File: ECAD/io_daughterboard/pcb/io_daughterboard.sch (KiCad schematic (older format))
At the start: 80 parts, among them P1 CONN_02X32, P2 CONN_02X32

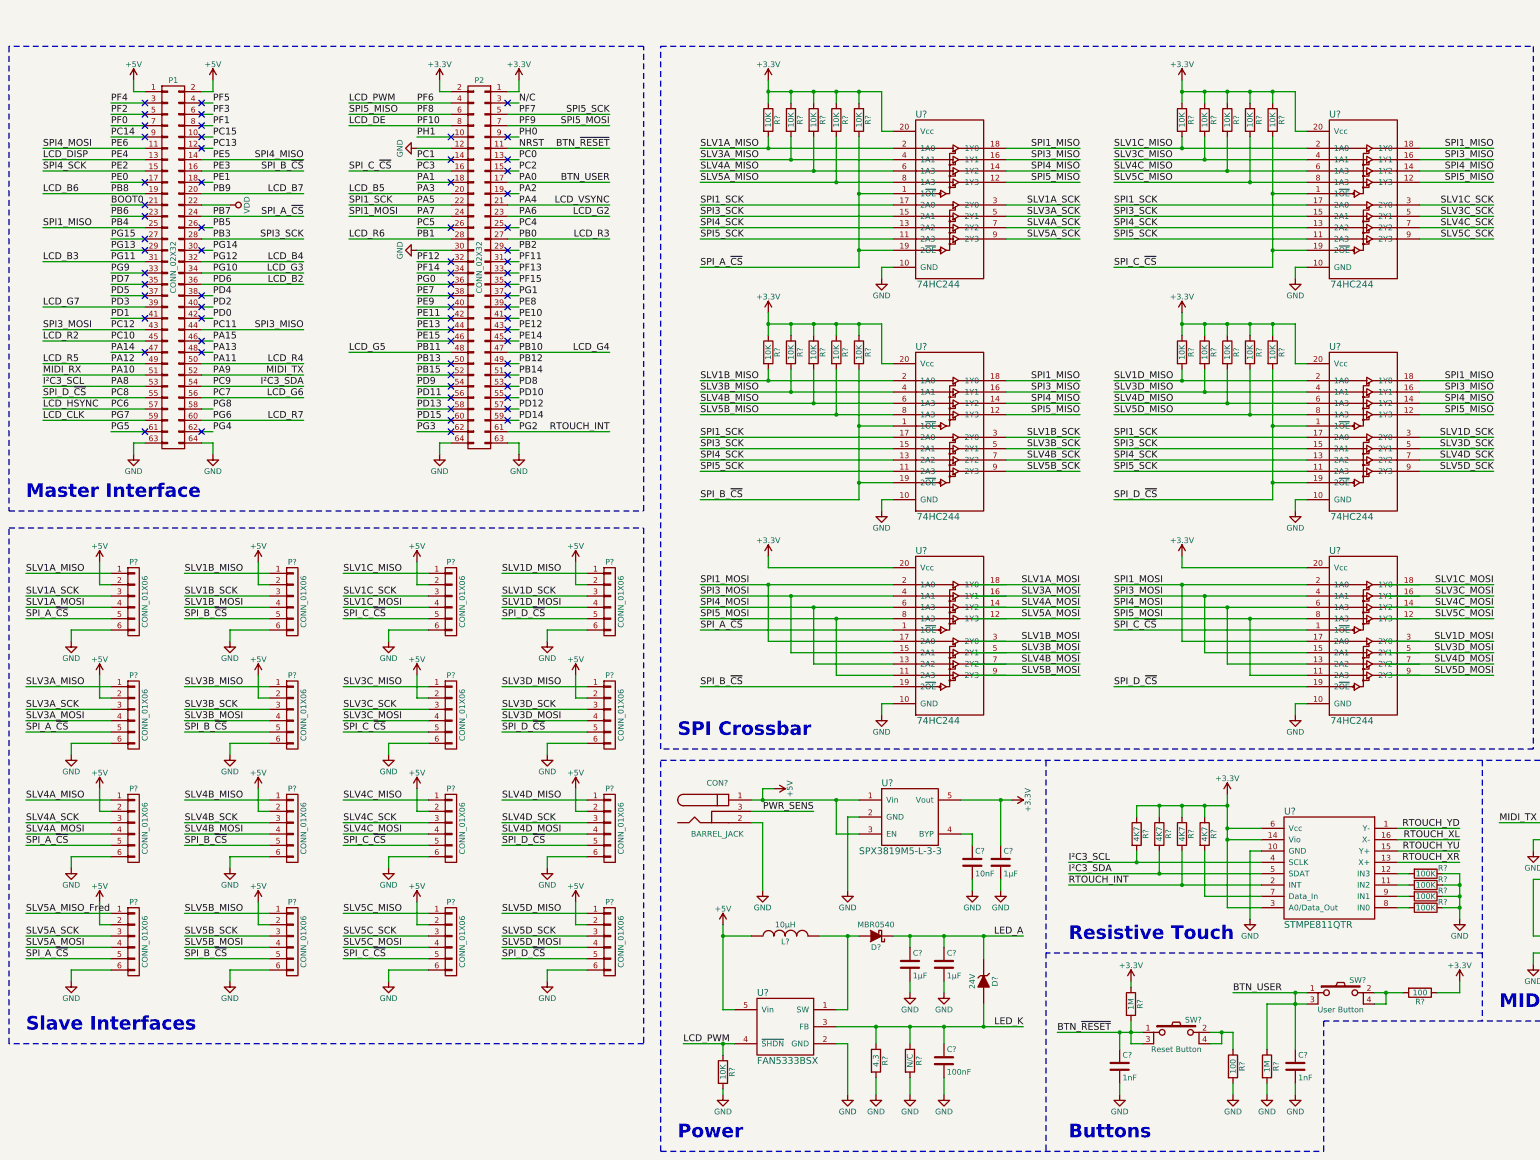
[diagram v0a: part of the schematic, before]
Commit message: Fixed 10 errors on schematic.  Still no power flags.
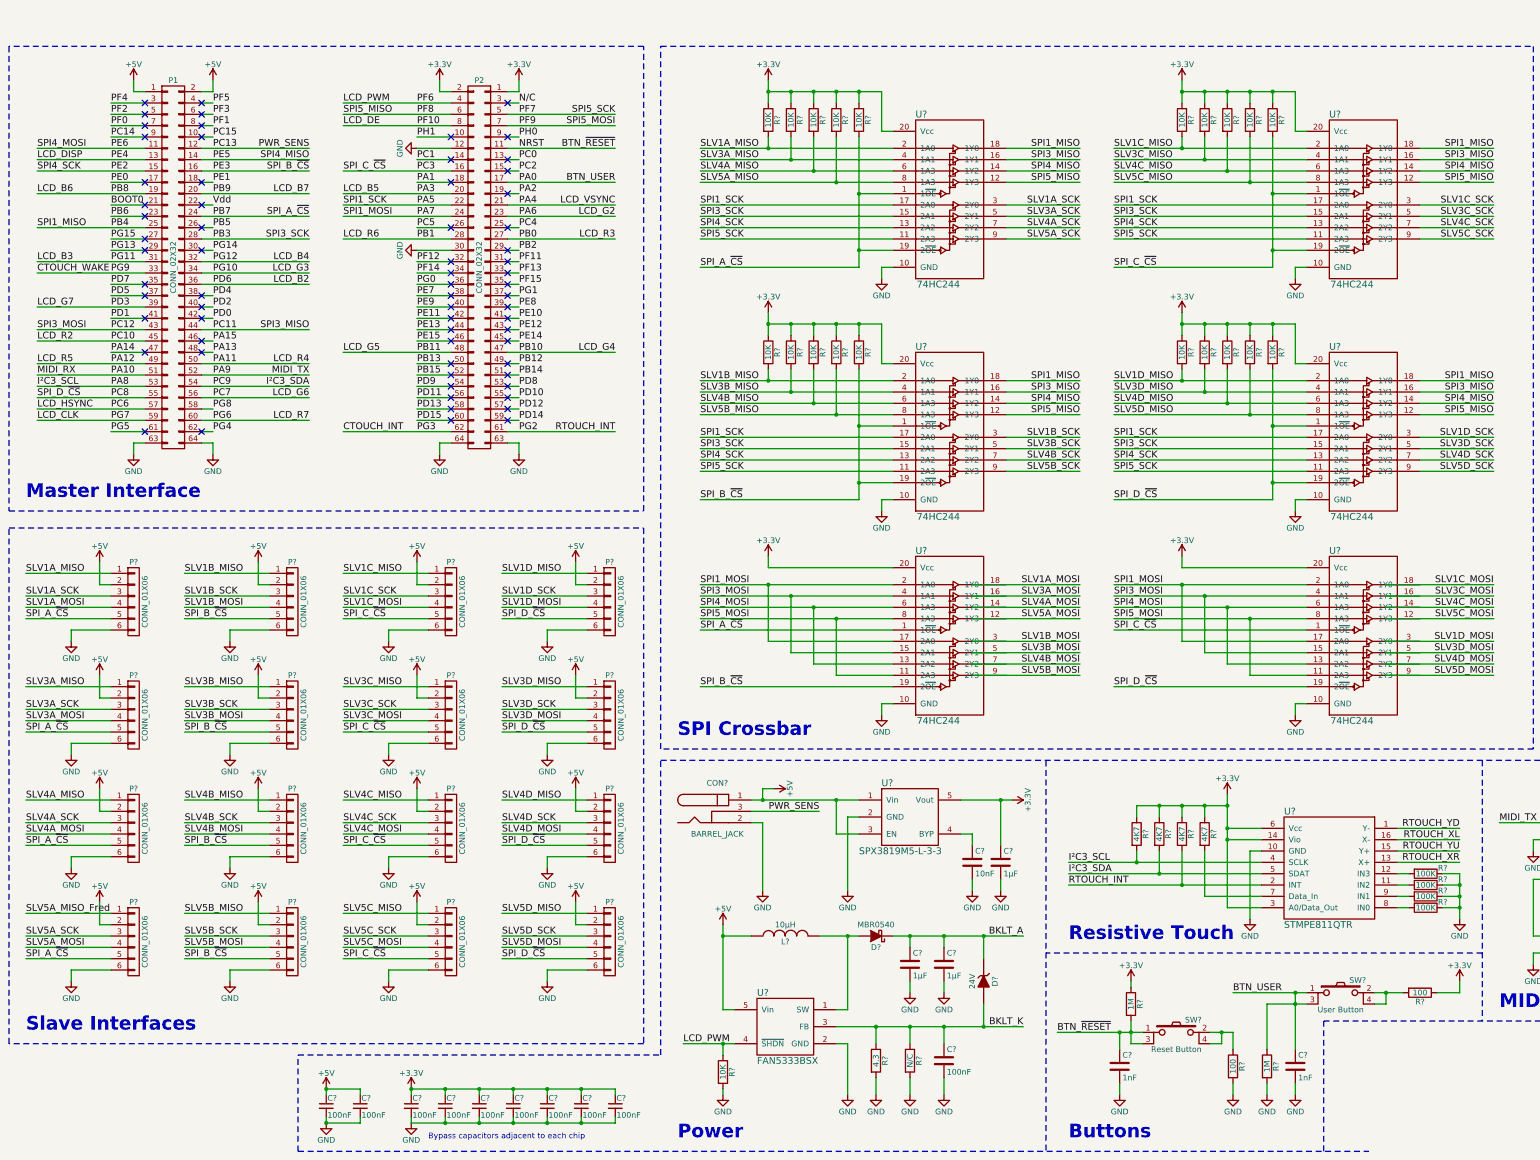
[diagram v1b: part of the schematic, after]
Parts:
- added C? (x9): 100nF, symbol C_Small
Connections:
- net LED_A is gone; now on net BKLT_A: C?.1, C?.1, D?.1 (K), D?.1 (K)
- net LED_K is gone; now on net BKLT_K: C?.1, D?.2 (A), R?.1, R?.1, U?.3 (FB)
- net PG3 is gone; now on net CTOUCH_INT: P2.62 (P62)
- net PG9 is gone; now on net CTOUCH_WAKE: P1.33 (P33)
- net PWR_SENS is gone; now on net PC13: CON?.3
- net +3V3: now also C?.1, C?.1, C?.1, C?.1, C?.1, C?.1, C?.1
- net +5V: now also C?.1, C?.1
- net GND: now also C?.2, C?.2, C?.2, C?.2, C?.2, C?.2, C?.2, C?.2, C?.2
- net VDD renamed Vdd
- no-connect marks 70 -> 68
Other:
- note added: "Bypass capacitors adjacent to each chip"

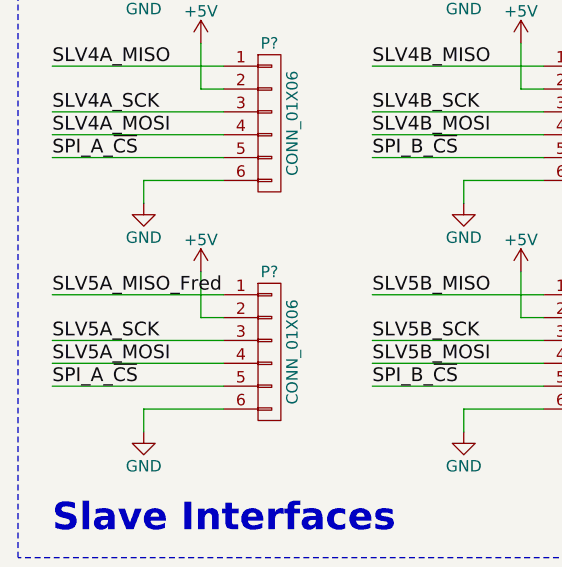
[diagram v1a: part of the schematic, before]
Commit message: Changed `SL5A_MISO_Fred` to `SL5A_MISO`.
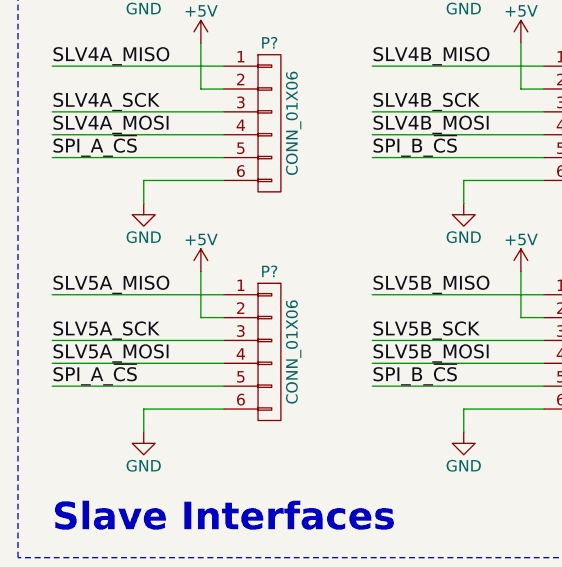
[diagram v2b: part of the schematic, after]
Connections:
- net SLV5A_MISO_Fred is gone; now on net SLV5A_MISO: P?.1 (P1)
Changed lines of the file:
@@
 $EndComp
 Text Label 800  8250 0    60   ~ 0
-SLV5A_MISO_Fred
+SLV5A_MISO
 Text Label 800  8450 0    60   ~ 0
 SLV5A_SCK

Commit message: Schematic annotated and electrical rules checked.
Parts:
- gave numbers to parts that had none: 87
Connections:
- net LCD_B6 is gone; now on net LCD_B0: J2.27 (B6), P1.19 (P19)
- net LCD_B7 is gone; now on net LCD_B1: J2.28 (B7), P1.20 (P20)
- net LCD_G6 is gone; now on net LCD_G0: J2.19 (G6), P1.56 (P56)
- net LCD_G7 is gone; now on net LCD_G1: J2.20 (G7), P1.39 (P39)
- net LCD_R6 is gone; now on net LCD_R0: J2.11 (R6), P2.28 (P28)
- net LCD_R7 is gone; now on net LCD_R1: J2.12 (R7), P1.60 (P60)
- net SLV1A_MOSI: now also U5.18 (1Y0)
- net SLV1B_MOSI: now also U5.3 (2Y0)
- net SLV1C_MOSI: now also U9.18 (1Y0)
- net SLV1D_MOSI: now also U9.3 (2Y0)
- net SLV3A_MOSI: now also U5.16 (1Y1)
- net SLV3B_MOSI: now also U5.5 (2Y1)
- net SLV3C_MOSI: now also U9.16 (1Y1)
- net SLV3D_MOSI: now also U9.5 (2Y1)
- net SLV4A_MOSI: now also U5.14 (1Y2)
- net SLV4B_MOSI: now also U5.7 (2Y2)
- net SLV4C_MOSI: now also U9.14 (1Y2)
- net SLV4D_MOSI: now also U9.7 (2Y2)
- net SLV5A_MOSI: now also U5.12 (1Y3)
- net SLV5B_MOSI: now also U5.9 (2Y3)
- net SLV5C_MOSI: now also U9.12 (1Y3)
- net SLV5D_MOSI: now also U9.9 (2Y3)
- no-connect marks 68 -> 69

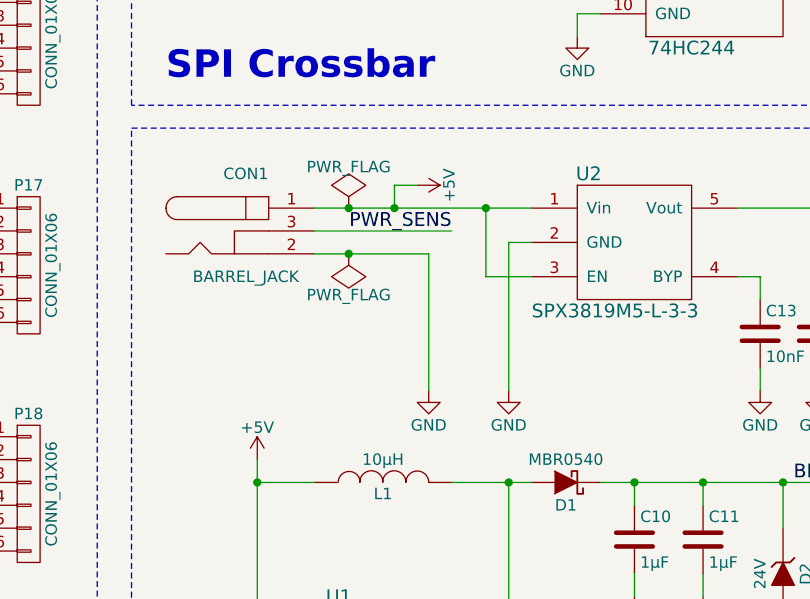
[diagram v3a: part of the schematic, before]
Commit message: Added footprints for the easy components.
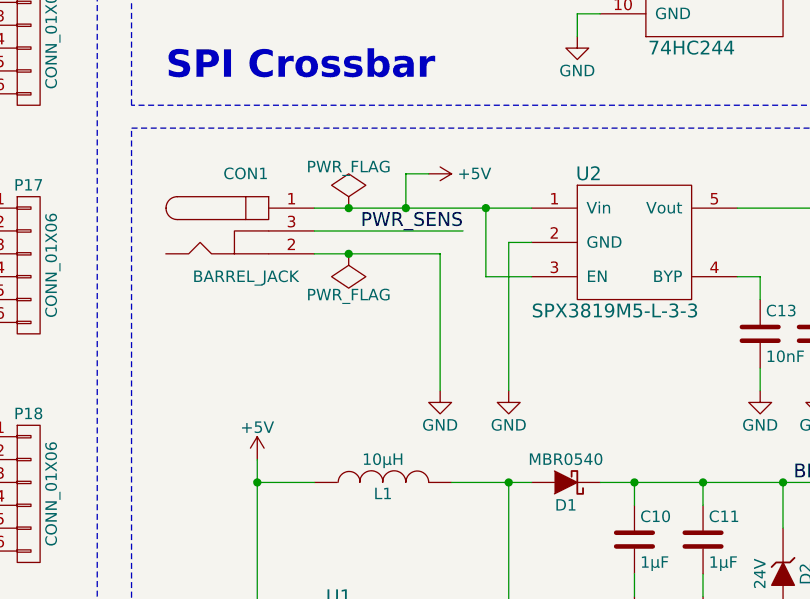
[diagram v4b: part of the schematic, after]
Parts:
- C1, C12, C13, C14, C15, C16, C2, C3, C4, C5, C6, C7, C8, C9: footprint (none) -> Capacitors_SMD:C_0603
- C10, C11: footprint (none) -> Capacitors_SMD:C_0805
- CON1: footprint (none) -> Connect:BARREL_JACK
- D1: footprint (none) -> Diodes_SMD:SOD-123
- D2: footprint (none) -> Diodes_SMD:SOD-323
- P1, P2: footprint (none) -> Socket_Strips:Socket_Strip_Straight_2x32
- R1, R10, R11, R14, R15, R16, R17, R18, R19, R2, R20, R21, R22, R23, R24, R25, R26, R27, R28, R29, R3, R30, R31, R32, R33, R34, R35, R4, R5, R6, R7, R8, R9: footprint (none) -> Resistors_SMD:R_0603
- R12, R13: footprint (none) -> Resistors_SMD:R_0603_HandSoldering
- U1, U10, U11, U2: footprint (none) -> TO_SOT_Packages_SMD:SOT-23-5
- U3, U4, U5, U7, U8, U9: footprint (none) -> Housings_SSOP:TSSOP-20_4.4x6.5mm_Pitch0.65mm
- U6: footprint (none) -> Housings_DFN_QFN:QFN-16-1EP_3x3mm_Pitch0.5mm

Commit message: Added I/O Daughter Board footprints.
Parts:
- J1: footprint (none) -> daughterfeet:XF2L-0625
- J2: footprint (none) -> daughterfeet:FPC_40
- L1: footprint (none) -> Inductors:Inductor_Taiyo-Yuden_NR-60xx
- P10, P11, P12, P13, P14, P15, P16, P17, P18, P3, P4, P5, P6, P7, P8, P9: footprint (none) -> daughterfeet:B6B-PH-SM4-TB
- P19: footprint (none) -> daughterfeet:B4B-PH-SM4-TB
- SW1, SW2: footprint (none) -> daughterfeet:WS-TASV
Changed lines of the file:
@@
 F 0 "P3" H 1750 5850 50  0000 C CNN
 F 1 "CONN_01X06" V 1850 5500 50  0000 C CNN
-F 2 "" H 1750 5500 50  0001 C CNN
+F 2 "daughterfeet:B6B-PH-SM4-TB" H 1750 5500 50  0001 C CNN
 F 3 "" H 1750 5500 50  0000 C CNN
 	1    1750 5500
@@
 F 0 "P19" H 16050 8050 50  0000 C CNN
 F 1 "CONN_01X04" V 16150 7800 50  0000 C CNN
-F 2 "" H 16050 7800 50  0001 C CNN
+F 2 "daughterfeet:B4B-PH-SM4-TB" H 16050 7800 50  0001 C CNN
 F 3 "" H 16050 7800 50  0000 C CNN
 	1    16050 7800
@@
 F 0 "J1" H 15350 1400 60  0000 L CNN
 F 1 "XF2L-0625-1A" H 15350 900 60  0000 L CNN
-F 2 "" H 15800 1400 60  0001 C CNN
+F 2 "daughterfeet:XF2L-0625" H 15800 1400 60  0001 C CNN
 F 3 "" H 15800 1400 60  0001 C CNN
 	1    15750 1300
@@
 F 0 "J2" H 13650 4300 60  0000 C CNN
 F 1 "4-1734839-0" H 13950 3800 60  0000 C CNN
-F 2 "" H 17050 4200 60  0001 C CNN
+F 2 "daughterfeet:FPC_40" H 17050 4200 60  0001 C CNN
 F 3 "" H 17050 4200 60  0001 C CNN
 	1    15800 4150
@@
 F 0 "SW2" H 12550 9060 50  0000 C CNN
 F 1 "User Button" H 12400 8800 50  0000 C CNN
-F 2 "" H 12400 8950 50  0001 C CNN
+F 2 "daughterfeet:WS-TASV" H 12400 8950 50  0001 C CNN
 F 3 "" H 12400 8950 50  0000 C CNN
 	1    12400 8950
@@
 F 0 "SW1" H 11100 9410 50  0000 C CNN
 F 1 "Reset Button" H 10950 9150 50  0000 C CNN
-F 2 "" H 10950 9300 50  0001 C CNN
+F 2 "daughterfeet:WS-TASV" H 10950 9300 50  0001 C CNN
 F 3 "" H 10950 9300 50  0000 C CNN
 	1    10950 9300
@@
 F 0 "L1" V 7450 8450 50  0000 C CNN
 F 1 "10µH" V 7600 8450 50  0000 C CNN
-F 2 "" H 7500 8450 50  0001 C CNN
+F 2 "Inductors:Inductor_Taiyo-Yuden_NR-60xx" H 7500 8450 50  0001 C CNN
 F 3 "" H 7500 8450 50  0000 C CNN
 	1    7500 8450
@@
 F 0 "P7" H 3150 5850 50  0000 C CNN
 F 1 "CONN_01X06" V 3250 5500 50  0000 C CNN
-F 2 "" H 3150 5500 50  0001 C CNN
+F 2 "daughterfeet:B6B-PH-SM4-TB" H 3150 5500 50  0001 C CNN
 F 3 "" H 3150 5500 50  0000 C CNN
 	1    3150 5500
@@
 F 0 "P11" H 4550 5850 50  0000 C CNN
 F 1 "CONN_01X06" V 4650 5500 50  0000 C CNN
-F 2 "" H 4550 5500 50  0001 C CNN
+F 2 "daughterfeet:B6B-PH-SM4-TB" H 4550 5500 50  0001 C CNN
 F 3 "" H 4550 5500 50  0000 C CNN
 	1    4550 5500
@@
 F 0 "P4" H 1750 6850 50  0000 C CNN
 F 1 "CONN_01X06" V 1850 6500 50  0000 C CNN
-F 2 "" H 1750 6500 50  0001 C CNN
+F 2 "daughterfeet:B6B-PH-SM4-TB" H 1750 6500 50  0001 C CNN
 F 3 "" H 1750 6500 50  0000 C CNN
 	1    1750 6500
@@
 F 0 "P8" H 3150 6850 50  0000 C CNN
 F 1 "CONN_01X06" V 3250 6500 50  0000 C CNN
-F 2 "" H 3150 6500 50  0001 C CNN
+F 2 "daughterfeet:B6B-PH-SM4-TB" H 3150 6500 50  0001 C CNN
 F 3 "" H 3150 6500 50  0000 C CNN
 	1    3150 6500
@@
 F 0 "P12" H 4550 6850 50  0000 C CNN
 F 1 "CONN_01X06" V 4650 6500 50  0000 C CNN
-F 2 "" H 4550 6500 50  0001 C CNN
+F 2 "daughterfeet:B6B-PH-SM4-TB" H 4550 6500 50  0001 C CNN
 F 3 "" H 4550 6500 50  0000 C CNN
 	1    4550 6500
@@
 F 0 "P15" H 5950 5850 50  0000 C CNN
 F 1 "CONN_01X06" V 6050 5500 50  0000 C CNN
-F 2 "" H 5950 5500 50  0001 C CNN
+F 2 "daughterfeet:B6B-PH-SM4-TB" H 5950 5500 50  0001 C CNN
 F 3 "" H 5950 5500 50  0000 C CNN
 	1    5950 5500
@@
 F 0 "P16" H 5950 6850 50  0000 C CNN
 F 1 "CONN_01X06" V 6050 6500 50  0000 C CNN
-F 2 "" H 5950 6500 50  0001 C CNN
+F 2 "daughterfeet:B6B-PH-SM4-TB" H 5950 6500 50  0001 C CNN
 F 3 "" H 5950 6500 50  0000 C CNN
 	1    5950 6500
@@
 F 0 "P5" H 1750 7850 50  0000 C CNN
 F 1 "CONN_01X06" V 1850 7500 50  0000 C CNN
-F 2 "" H 1750 7500 50  0001 C CNN
+F 2 "daughterfeet:B6B-PH-SM4-TB" H 1750 7500 50  0001 C CNN
 F 3 "" H 1750 7500 50  0000 C CNN
 	1    1750 7500
@@
 F 0 "P9" H 3150 7850 50  0000 C CNN
 F 1 "CONN_01X06" V 3250 7500 50  0000 C CNN
-F 2 "" H 3150 7500 50  0001 C CNN
+F 2 "daughterfeet:B6B-PH-SM4-TB" H 3150 7500 50  0001 C CNN
 F 3 "" H 3150 7500 50  0000 C CNN
 	1    3150 7500
@@
 F 0 "P13" H 4550 7850 50  0000 C CNN
 F 1 "CONN_01X06" V 4650 7500 50  0000 C CNN
-F 2 "" H 4550 7500 50  0001 C CNN
+F 2 "daughterfeet:B6B-PH-SM4-TB" H 4550 7500 50  0001 C CNN
 F 3 "" H 4550 7500 50  0000 C CNN
 	1    4550 7500
@@
 F 0 "P6" H 1750 8850 50  0000 C CNN
 F 1 "CONN_01X06" V 1850 8500 50  0000 C CNN
-F 2 "" H 1750 8500 50  0001 C CNN
+F 2 "daughterfeet:B6B-PH-SM4-TB" H 1750 8500 50  0001 C CNN
 F 3 "" H 1750 8500 50  0000 C CNN
 	1    1750 8500
@@
 F 0 "P10" H 3150 8850 50  0000 C CNN
 F 1 "CONN_01X06" V 3250 8500 50  0000 C CNN
-F 2 "" H 3150 8500 50  0001 C CNN
+F 2 "daughterfeet:B6B-PH-SM4-TB" H 3150 8500 50  0001 C CNN
 F 3 "" H 3150 8500 50  0000 C CNN
 	1    3150 8500
@@
 F 0 "P14" H 4550 8850 50  0000 C CNN
 F 1 "CONN_01X06" V 4650 8500 50  0000 C CNN
-F 2 "" H 4550 8500 50  0001 C CNN
+F 2 "daughterfeet:B6B-PH-SM4-TB" H 4550 8500 50  0001 C CNN
 F 3 "" H 4550 8500 50  0000 C CNN
 	1    4550 8500
@@
 F 0 "P17" H 5950 7850 50  0000 C CNN
 F 1 "CONN_01X06" V 6050 7500 50  0000 C CNN
-F 2 "" H 5950 7500 50  0001 C CNN
+F 2 "daughterfeet:B6B-PH-SM4-TB" H 5950 7500 50  0001 C CNN
 F 3 "" H 5950 7500 50  0000 C CNN
 	1    5950 7500
@@
 F 0 "P18" H 5950 8850 50  0000 C CNN
 F 1 "CONN_01X06" V 6050 8500 50  0000 C CNN
-F 2 "" H 5950 8500 50  0001 C CNN
+F 2 "daughterfeet:B6B-PH-SM4-TB" H 5950 8500 50  0001 C CNN
 F 3 "" H 5950 8500 50  0000 C CNN
 	1    5950 8500
